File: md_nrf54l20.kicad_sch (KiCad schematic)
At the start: 31 parts, among them J1 USB_C, J2 SWD, Q1 BSS138DW, U1 nRF54L20, U2 AMS1117-3.3, U3 CH347T, Y1 8MHz, Y2 32MHz

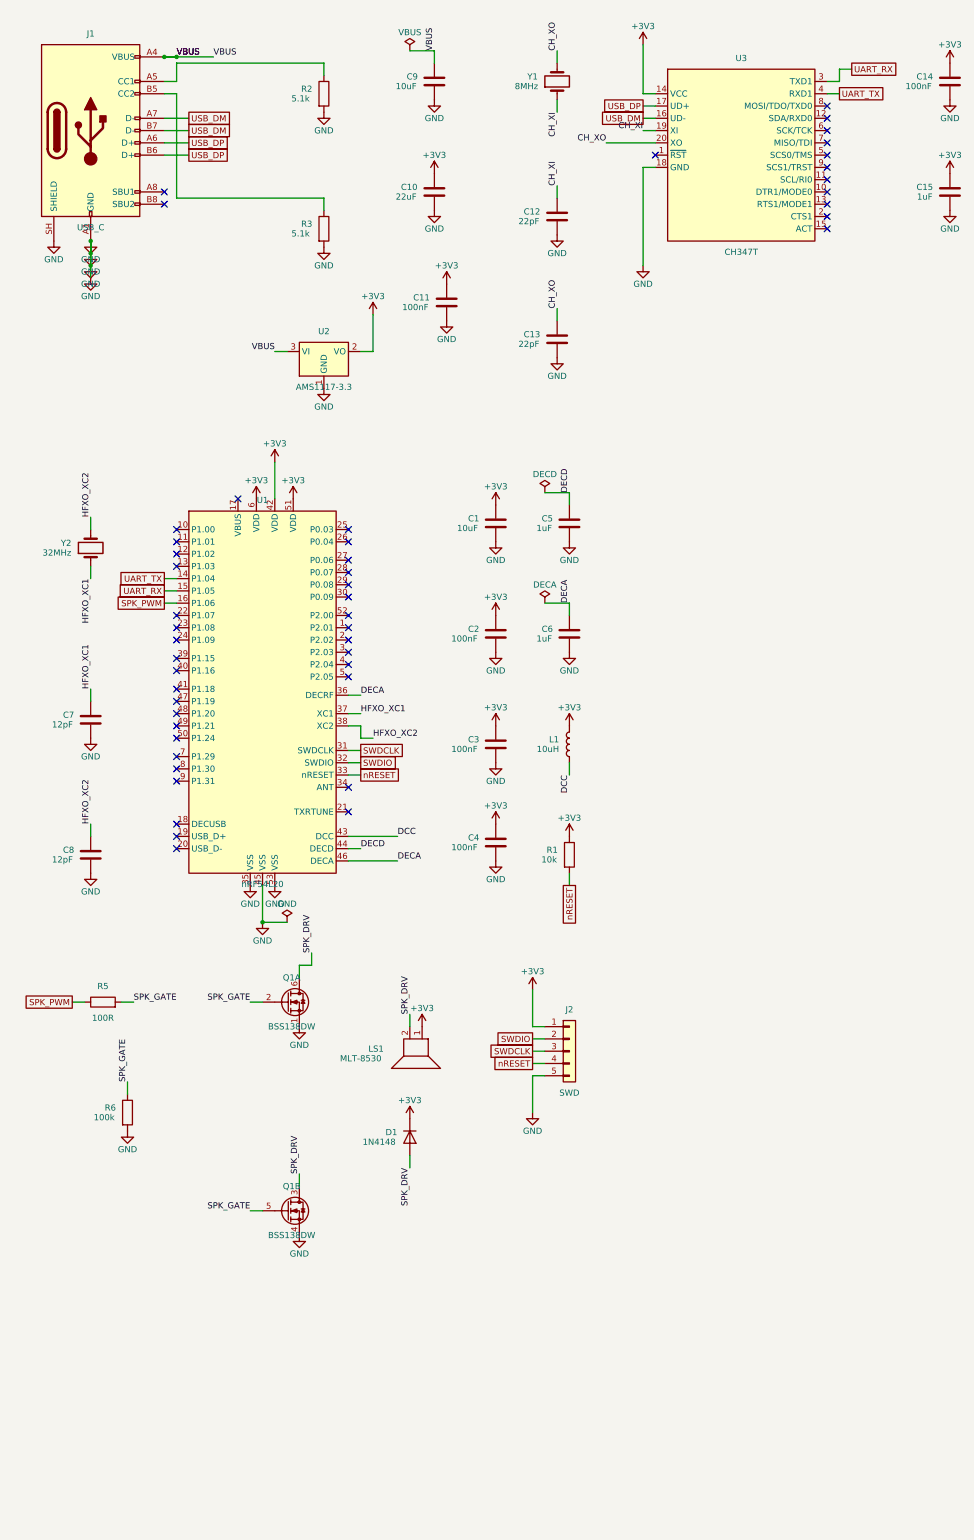
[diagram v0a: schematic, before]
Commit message: Promote v2 and add Uno R3 shield headers
- circuit_v2.json -> circuit.json (single source); generated to the project
  root md_nrf54l20.kicad_sch; md_nrf54l20-v2.kicad_sch removed.
- Board: copied the ~/uno R3 form-factor PCB over md_nrf54l20.kicad_pcb
  (J1-J4 header sockets + 4 mounting holes); added Arduino_MountingHole.pretty
  and registered it in fp-lib-table.
- Wired the Uno headers to the nRF with function-correct pins: A0-A5 on ADC
  channels (AIN0-4 + AIN7), AREF on EXTREF, UART on D0/D1, SPI on D10-D13,
  PWM-capable pins on D3/D5/D6/D9/D10/D11; I2C SDA/SCL shared with A4/A5.
- Renumbered existing connectors so the Uno headers can be J1-J4: USB-C -> J5,
  SWD -> J6. Moved speaker PWM P1.06 -> P2.01 to free P1.06 for analog A4.

Co-Authored-By: Claude Opus 4.8 <noreply@anthropic.com>
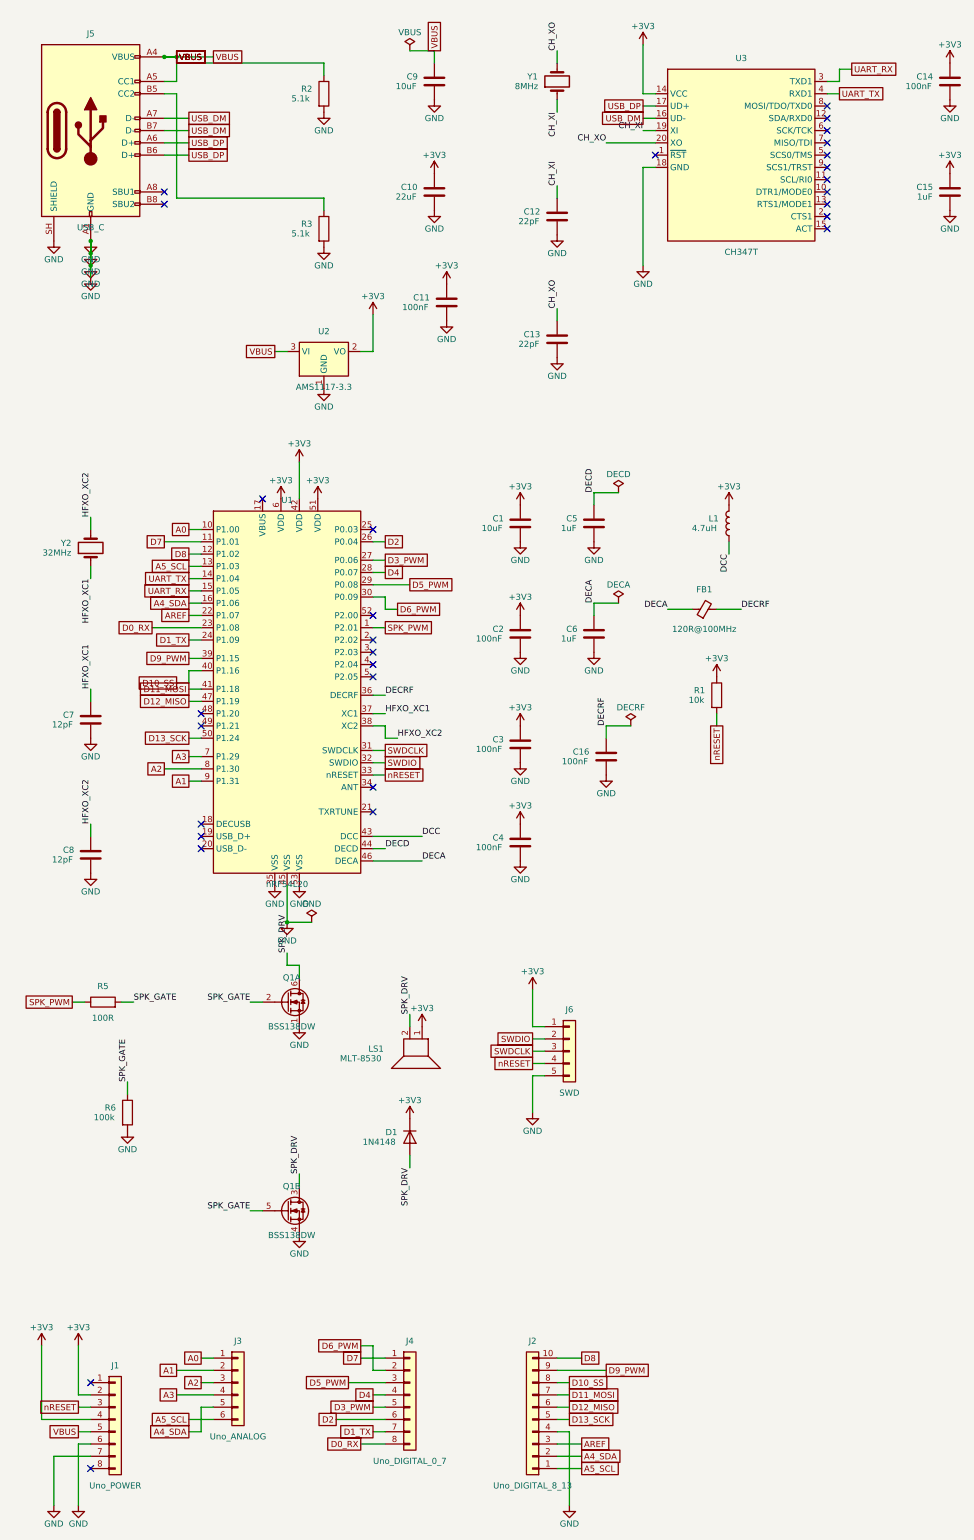
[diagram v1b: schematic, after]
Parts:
- added C16: 100nF, Capacitor_SMD:C_0603_1608Metric, symbol Device:C
- added FB1: 120R@100MHz, Inductor_SMD:L_0603_1608Metric, symbol Device:FerriteBead_Small
- added J3: Uno_ANALOG, Connector_PinSocket_2.54mm:PinSocket_1x06_P2.54mm_Vertical, symbol Connector_Generic:Conn_01x06
- added J4: Uno_DIGITAL_0_7, Connector_PinSocket_2.54mm:PinSocket_1x08_P2.54mm_Vertical, symbol Connector_Generic:Conn_01x08
- added J5: USB_C, Connector_USB:USB_C_Receptacle_GCT_USB4105-xx-A_16P_TopMnt_Horizontal, symbol Connector:USB_C_Receptacle_USB2.0_16P
- added J6: SWD, Connector_PinHeader_2.54mm:PinHeader_1x05_P2.54mm_Vertical, symbol Connector_Generic:Conn_01x05
- J1: value USB_C -> Uno_POWER; footprint Connector_USB:USB_C_Receptacle_GCT_USB4105-xx-A_16P_TopMnt_Horizontal -> Connector_PinSocket_2.54mm:PinSocket_1x08_P2.54mm_Vertical; symbol Connector:USB_C_Receptacle_USB2.0_16P -> Connector_Generic:Conn_01x08
- J2: value SWD -> Uno_DIGITAL_8_13; footprint Connector_PinHeader_2.54mm:PinHeader_1x05_P2.54mm_Vertical -> Connector_PinSocket_2.54mm:PinSocket_1x10_P2.54mm_Vertical; symbol Connector_Generic:Conn_01x05 -> Connector_Generic:Conn_01x10
- L1: value 10uH -> 4.7uH; footprint Inductor_SMD:L_1210_3225Metric -> Inductor_SMD:L_0603_1608Metric
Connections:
- net +3V3: now also J1.2 (Pin_2), J1.4 (Pin_4), J6.1 (Pin_1); no longer J2.1 (Pin_1)
- net DECA: now also FB1.1; no longer U1.36 (DECRF)
- net GND: now also J1.6 (Pin_6), J1.7 (Pin_7), J2.4 (Pin_4), C16.2, J5.A1 (GND), J5.A12 (GND), J5.B1 (GND), J5.B12 (GND), J5.SH (SHIELD), J6.5 (Pin_5); no longer J1.A1 (GND), J1.A12 (GND), J1.B1 (GND), J1.B12 (GND), J1.SH (SHIELD), J2.5 (Pin_5)
- net SPK_PWM: now also U1.1 (P2.01); no longer U1.16 (P1.06)
- net SWDCLK: now also J6.3 (Pin_3); no longer J2.3 (Pin_3)
- net SWDIO: now also J6.2 (Pin_2); no longer J2.2 (Pin_2)
- net USB_DM: now also J5.A7 (D-), J5.B7 (D-); no longer J1.A7 (D-), J1.B7 (D-)
- net USB_DP: now also J5.A6 (D+), J5.B6 (D+); no longer J1.A6 (D+), J1.B6 (D+)
- net VBUS: now also J1.5 (Pin_5), J5.A4 (VBUS), J5.A9 (VBUS), J5.B4 (VBUS), J5.B9 (VBUS); no longer J1.A4 (VBUS), J1.A9 (VBUS), J1.B4 (VBUS), J1.B9 (VBUS)
- net nRESET: now also J1.3 (Pin_3), J6.4 (Pin_4); no longer J2.4 (Pin_4)
- net at R3.1: now also J5.B5 (CC2); no longer J1.B5 (CC2)
- net A0: now reaches U1.10 (P1.00)
- net A0: now also J3.1 (Pin_1)
- net D7: now reaches U1.11 (P1.01)
- net D7: now also J4.1 (Pin_1)
- net D8: now reaches U1.12 (P1.02)
- net D8: now also J2.10 (Pin_10)
- net A5_SCL: now reaches U1.13 (P1.03)
- net A5_SCL: now also J2.1 (Pin_1), J3.6 (Pin_6)
- net AREF: now reaches U1.22 (P1.07)
- net AREF: now also J2.3 (Pin_3)
- net D0_RX: now reaches U1.23 (P1.08)
- net D0_RX: now also J4.8 (Pin_8)
- net D1_TX: now reaches U1.24 (P1.09)
- net D1_TX: now also J4.7 (Pin_7)
- net D2: now reaches U1.26 (P0.04)
- net D2: now also J4.6 (Pin_6)
- net D3_PWM: now reaches U1.27 (P0.06)
- net D3_PWM: now also J4.5 (Pin_5)
- net D4: now reaches U1.28 (P0.07)
- net D4: now also J4.4 (Pin_4)
- net D5_PWM: now reaches U1.29 (P0.08)
- net D5_PWM: now also J4.3 (Pin_3)
- net D6_PWM: now reaches U1.30 (P0.09)
- net D6_PWM: now also J4.2 (Pin_2)
- net D9_PWM: now reaches U1.39 (P1.15)
- net D9_PWM: now also J2.9 (Pin_9)
- net D10_SS: now reaches U1.40 (P1.16)
- net D10_SS: now also J2.8 (Pin_8)
- net D11_MOSI: now reaches U1.41 (P1.18)
- net D11_MOSI: now also J2.7 (Pin_7)
- net D12_MISO: now reaches U1.47 (P1.19)
- net D12_MISO: now also J2.6 (Pin_6)
- net D13_SCK: now reaches U1.50 (P1.24)
- net D13_SCK: now also J2.5 (Pin_5)
- net A3: now reaches U1.7 (P1.29)
- net A3: now also J3.4 (Pin_4)
- net A2: now reaches U1.8 (P1.30)
- net A2: now also J3.3 (Pin_3)
- net A1: now reaches U1.9 (P1.31)
- net A1: now also J3.2 (Pin_2)
- net at R2.1: now also J5.A5 (CC1); no longer J1.A5 (CC1)
- new net A4_SDA: J2.2 (Pin_2), J3.5 (Pin_5), U1.16 (P1.06)
- new net DECRF: C16.1, FB1.2, U1.36 (DECRF)
- no-connect marks 49 -> 30
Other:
- title: md_nrf54l20 - USB / CH347 / speaker -> md_nrf54l20 - USB / CH347 / speaker / Uno shield
- moved on the sheet: C1, C2, C3, C4, C5, C6, L1, R1, U1
